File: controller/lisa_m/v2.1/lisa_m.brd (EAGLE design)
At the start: 50.7 x 33.6 mm, 119 parts, among them IC9 LP2992 5V, J1 CONN_3-1, J2 CONN_3-1, J3 CONN_3-1, J4 CONN_3-1, J5 CONN_3-1, J6 CONN_3-1, J7 CONN_3-1, J8 CONN_3-1, Q1 12Mhz, U1 MCP2551SN, U2 STM32-C-64, U3 BMP085

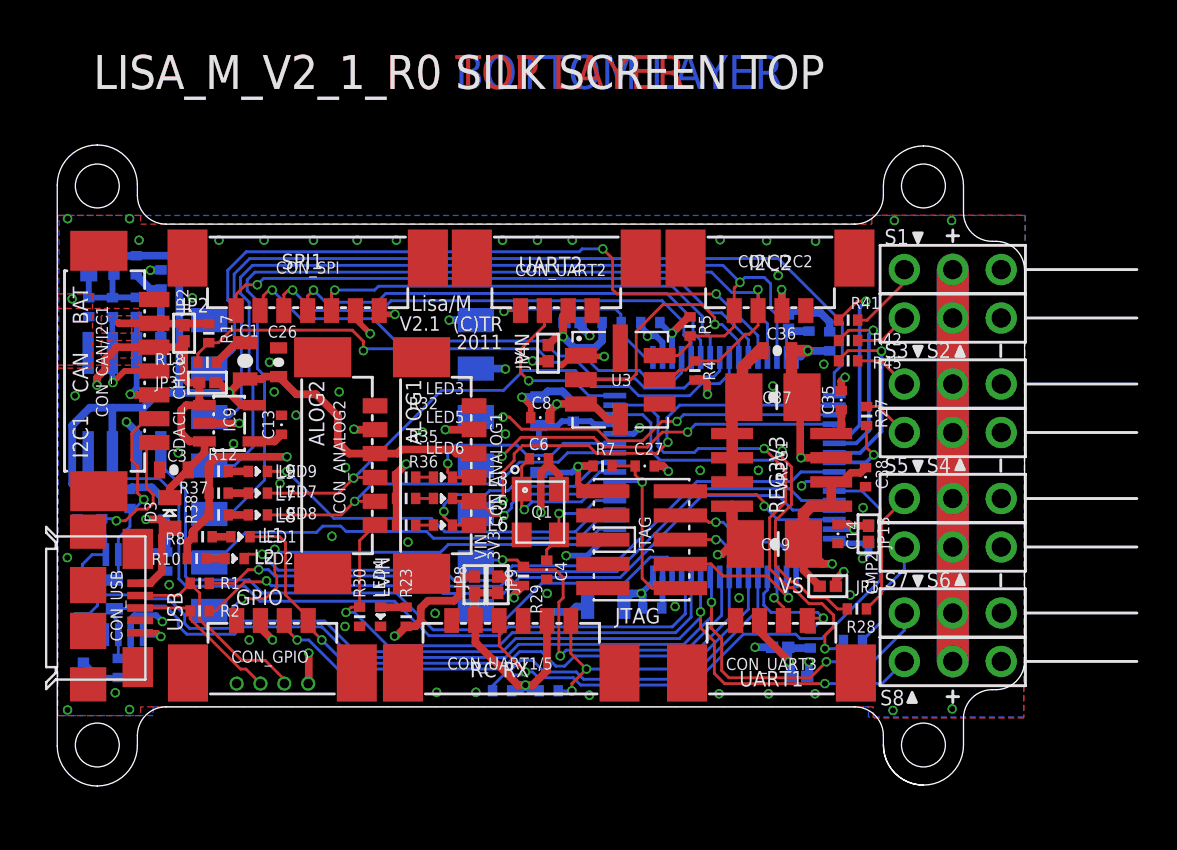
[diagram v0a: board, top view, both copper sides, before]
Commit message: Updated V2.1 Lisa/M(X) hardware to the final production version.
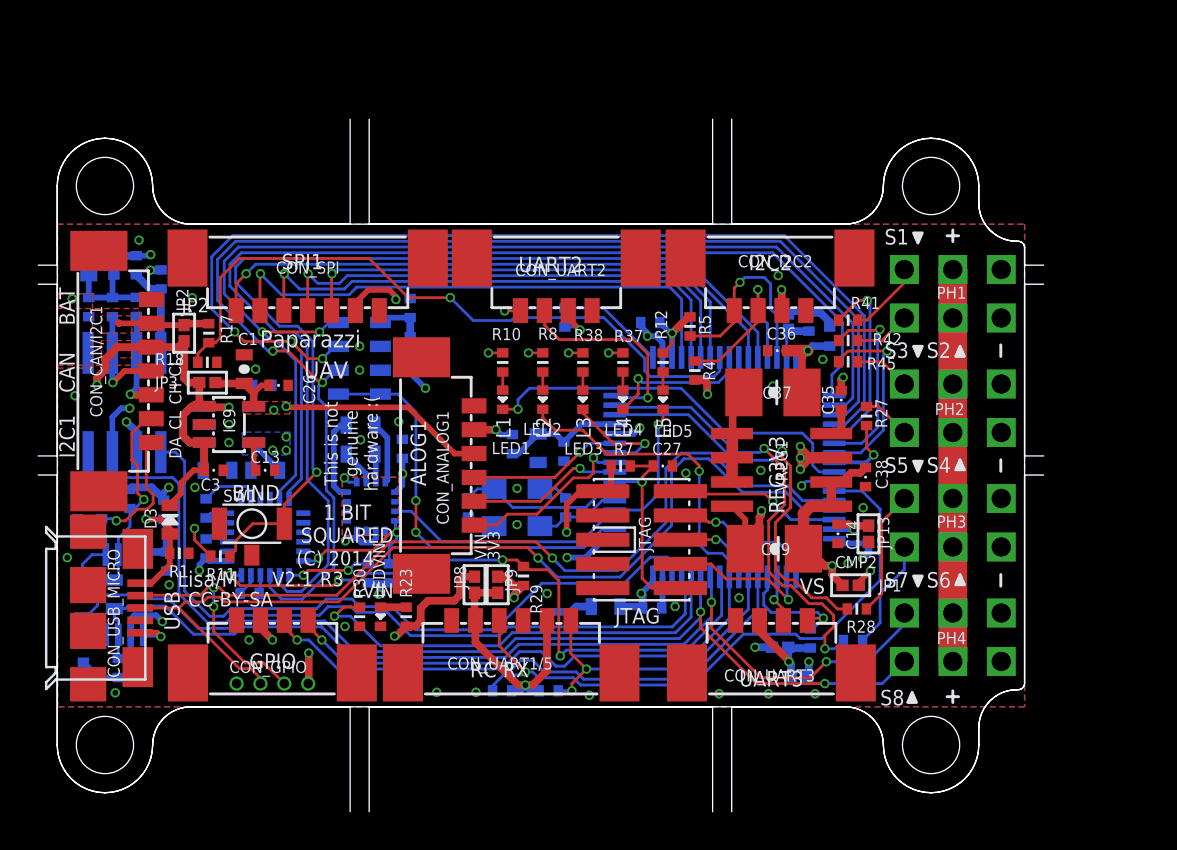
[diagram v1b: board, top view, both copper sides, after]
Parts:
- removed C8: 100n, pel_dipol_comp:0402-CAP
- removed CON_ANALOG2: (no value), pel_molex:PB-53398-06
- removed IMU: ASPIRIN, joby_robotics:ASPIRIN_1
- removed J1, J2, J3, J4, J5, J6, J7, J8: CONN_3-1, pel_misc:SIP1X3_100
- removed JP4, JP5: 0/DNP, pel_jumpers:0402-SQJMP
- removed LED6, LED7, LED8, LED9: BLU, pel_dipol_comp:0402-LED
- removed R32, R35, R36: 80R, pel_dipol_comp:0402-RES
- removed U$1: TR-LOGO, quadshot:TR-LOGO
- removed U3: BMP085, omc:LCC8
- added C101, C108, C110, C112: 100n, pel_dipol_comp:0402-CAP
- added C104: 2u2, pel_dipol_comp:0603-CAP
- added C105, C113: 4u7, pel_dipol_comp:0603-CAP
- added C106: 10n, pel_dipol_comp:0402-CAP
- added C109: 2n2, pel_dipol_comp:0402-CAP
- added C114: 220n, pel_dipol_comp:0603-CAP
- added IC101: LP2992, v-reg-micrel:SOT23-5
- added IC102: MS5611, aspirin:QFN-MS5611
- added L101: L, pel_dipol_comp:0402-IND
- added LEDVIN: GRN, pel_dipol_comp:0402-LED
- added PH1, PH2, PH3, PH4: PH2X3, pel_hdr:PH010-2-3
- added R11, R9: 2k2, pel_dipol_comp:0402-RES
- added SW1: MICROTACT_GND, paparazzi:MICROTACT_GND
- added U102: MPU-6000, aspirin:QFN24-NO-PAD
- added U103: HMC5883L, aspirin:LPCC16-HMC5883L
- C1, C9: device pel_dipol_comp:0805-CAP -> pel_dipol_comp:0603-CAP
- C26, C3, C36: device pel_dipol_comp:0603-CAP -> pel_dipol_comp:0402-CAP
- C28: device pel_dipol_comp:0603-POL-CAP -> pel_dipol_comp:0603-CAP
- C4, C6: value 30p -> 10p
- CON_CAN/I2C1: device pel_molex:PB-53261-07 -> pel_molex:PB-53398-07
- D3: device diode:MICROMELF-R -> pel_dipol_comp:0603-DIO
- L1: value (none) -> L; device res_cap:0603-IND -> pel_dipol_comp:0402-IND
- LED2: value BLU -> ORG
- LED3: value BLU -> GRN
- LED4: value ORG -> YEL
- LED5: value BLU -> RED
- R1: value 22R -> 10k
- R10, R12, R37, R38: value 80R -> 300
- R18, R23: value 2k -> 2k2
- R2: value 22R -> 2k2
- R24, R26, R29, R3, R30, R6: value 2k7 -> 10k
- R33, R34, R4, R5: value 2k7 -> 2k2
- R43, R44: value 1k5 -> 2k2
- R8: value 300R -> 300
- moved R12 24.0 mm to (31.8, 18.1), turned to 90 degrees
- moved R37 22.3 mm to (29.6, 18.1), turned to 90 degrees
- moved R38 20.7 mm to (27.6, 18.1), turned to 90 degrees
- moved R8 20.0 mm to (25.4, 18.1), turned to 90 degrees
- moved R10 19.0 mm to (23.4, 18.1), turned to 90 degrees
- moved LED2 18.2 mm to (25.4, 16.1), turned to 270 degrees
- moved LED4 17.1 mm to (29.6, 16.1)
- moved LED1 15.5 mm to (23.4, 16.1), turned to 270 degrees
- moved LED5 12.6 mm to (31.8, 16.1), turned to 270 degrees
- moved R2 10.1 mm to (17.4, 7.00), flipped to the bottom, turned to 270 degrees
- moved LED3 8.38 mm to (27.6, 16.1), turned to 270 degrees
- moved C6 4.49 mm to (21.6, 10.4), flipped to the bottom, turned to 270 degrees
- moved C4 3.41 mm to (26.6, 10.4), flipped to the bottom, turned to 270 degrees
- moved C13 2.53 mm to (10.9, 12.4), turned to 0 degrees
- moved R26 2.46 mm to (26.6, 20.4), turned to 90 degrees
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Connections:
- removed net ADC_4: CON_ANALOG2.4, LED7.C, U2.25
- removed net ADC_6: CON_ANALOG2.5, LED8.C, U2.10
- removed net FT_USB_DM: CON_USB.2, CON_USB_MICRO.PIN_2, R1.P$1
- removed net FT_USB_DP: CON_USB.3, CON_USB_MICRO.PIN_3, R2.P$1
- removed net IMU_ACC_CS: IMU.P$12, U2.33
- removed net IMU_ACC_DRDY: IMU.P$13, U2.28
- removed net IMU_GYRO_DRDY: IMU.P$9, U2.3
- removed net IMU_GYRO_SS: IMU.P$8, U2.2
- removed net IMU_MAG_DRDY: IMU.P$6, R29.P$2, U2.57
- removed net JTAG_TRST: CON_GPIO.4, LED1.C, U2.56
- removed net N$11: LED6.A, R36.P$1
- removed net N$9: LED5.A, R35.P$1
- removed net U2_POW: CON_UART2.2, JP4.P$2, JP5.P$2, R26.P$1
- new net BARO_+3V3: C101.P$1, IC102.1, L101.P$1
- new net BIND_BUT: R11.P$2, SW1.2, U2.28
- new net IMU+3V3: C105.P$1, C108.P$1, C112.P$1, IC101.5, L101.P$2, U102.13, U103.13, U103.2, U103.4
- new net IMU_BARO_CS: IC102.4, IC102.5, U2.2
- new net IMU_MAG_INT: U103.15, U2.3
- new net IMU_MPU_CS: U102.8, U2.33
- new net IMU_MPU_INT: R29.P$2, U102.12, U2.57
- new net LED3: LED3.C, U2.10
- new net LED4: LED4.C, U2.25
- new net LED5: LED5.C, U2.4
- new net N$19: C106.P$2, IC101.4
- new net N$2: C109.P$1, U102.20
- new net N$3: C110.P$1, U102.10
- new net N$34: C114.P$2, U103.8
- new net N$48: C114.P$1, U103.12
- new net SCL: R9.P$1, U102.7, U103.1
- new net SDA: R2.P$1, U102.6, U103.16
- net +3V3: now also CON_UART2.2, R11.P$1, R2.P$2, R26.P$1, R9.P$2; no longer C8.P$2, CON_ANALOG2.2, JP5.P$1, R32.P$2, R35.P$2, R36.P$2, U3.3, U3.4
- net +5V: no longer CON_ANALOG2.3
- net ADC_1: no longer LED3.C
- net ADC_2: no longer LED5.C
- net ADC_3: no longer LED6.C
- net BARO_DRDY: no longer U3.2
- net BOOT0: no longer CON_ANALOG2.6
- net GND: now also C101.P$2, C104.P$2, C105.P$2, C106.P$1, C108.P$2, C109.P$2, C110.P$2, C112.P$2, C113.P$2, C28.P$2, IC101.2, IC102.2, IC102.3, LEDVIN.C, PH1.3, PH1.6, PH2.3, PH2.6, PH3.3, PH3.6, PH4.3, PH4.6, R1.P$2, SW1.1, SW1.G, U102.1, U102.11, U102.18, U103.11, U103.9; no longer C28.-, C8.P$1, CON_ANALOG2.1, IMU.P$1, IMU.P$14, IMU.P$7, J1.1, J2.1, J3.1, J4.1, J5.1, J6.1, J7.1, J8.1, LED4.C, U3.1
- net I2C2_SCL: no longer IMU.P$10, U3.6
- net I2C2_SDA: no longer IMU.P$11, U3.7
- net IMU_SPI_MISO: now also IC102.6, U102.9; no longer IMU.P$3
- net IMU_SPI_MOSI: now also IC102.7, U102.24; no longer IMU.P$4
- net IMU_SPI_SCK: now also IC102.8, U102.23; no longer IMU.P$5
- net LED1: now also LED1.C; no longer LED2.C
- net LED2: now also CON_GPIO.4, LED2.C, U2.56; no longer LED9.C, U2.4
- net N$10: now also LED2.A; no longer LED1.A
- net N$12: now also LEDVIN.A; no longer LED4.A
- net N$13: now also LED5.A; no longer LED9.A
- net N$14: now also LED4.A; no longer LED7.A
- net N$15: now also LED3.A; no longer LED8.A
- net N$4: now also LED1.A; no longer LED2.A
- net N$5: now also C113.P$1, U103.10; no longer LED3.A, R32.P$1
- net S1: now also PH1.1; no longer J1.3
- net S2: now also PH1.4; no longer J2.3
- net S3: now also PH2.1; no longer J3.3
- net S4: now also PH2.4; no longer J4.3
- net S5: now also PH3.1; no longer J5.3
- net S6: now also PH3.4; no longer J6.3
- net S7: now also PH4.1; no longer J7.3
- net S8: now also PH4.4; no longer J8.3
- net SERVO_BUS: now also PH1.2, PH1.5, PH2.2, PH2.5, PH3.2, PH3.5, PH4.2, PH4.5; no longer J1.2, J2.2, J3.2, J4.2, J5.2, J6.2, J7.2, J8.2
- net USB_DM: now also CON_USB.2, CON_USB_MICRO.PIN_2; no longer R1.P$2
- net USB_DP: now also CON_USB.3, CON_USB_MICRO.PIN_3; no longer R2.P$2
- net USB_VBUS: now also R1.P$1
- net VDDA: now also C28.P$1; no longer C28.+
- net V_IN: now also C104.P$1, IC101.1, IC101.3; no longer IMU.P$2, JP4.P$1
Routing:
- net IMU_MPU_CS: track 0.00 -> 60.2 mm
- net BIND_BUT: track 0.00 -> 50.8 mm, vias 0 -> 1
- net IMU_SPI_MISO: track 19.9 -> 67.1 mm
- net IMU_ACC_CS: track 46.6 -> 0.00 mm
- net I2C2_SCL: track 53.9 -> 9.61 mm
- net IMU_SPI_MOSI: track 20.1 -> 62.6 mm, vias 2 -> 3
- net I2C2_SDA: track 51.7 -> 10.7 mm
- net IMU_ACC_DRDY: track 38.3 -> 0.00 mm, vias 2 -> 0
- net IMU_SPI_SCK: track 23.4 -> 58.6 mm
- net IMU_MPU_INT: track 0.00 -> 34.4 mm, vias 0 -> 4
- net JTAG_TRST: track 33.5 -> 0.00 mm, vias 1 -> 0
- net ADC_4: track 29.9 -> 0.00 mm, vias 1 -> 0
- net IMU_GYRO_SS: track 24.5 -> 0.00 mm, vias 2 -> 0
- net +5V: track 49.1 -> 25.5 mm, vias 1 -> 5
- net LED2: track 20.0 -> 43.6 mm, vias 1 -> 2
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- added copper zone on layer 1, net +5V
- added copper zone on layer 15, net +5V
- added copper zone on layer 15, net IMU+3V3
- added copper zone on layer 16, net IMU+3V3
- added copper zone on layer 1, net N$11
- added copper zone on layer 15, net N$11
- added copper zone on layer 16, net N$11
- added copper zone on layer 2, net N$11
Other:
- board size 50.7 x 33.6 mm -> 52.7 x 36.3 mm
- board text added: "(C) 2010-2015 Piotr Esden-Tempski <piotr@esden.net>"
- board text added: "(C) 2014"
- board text added: "(C)1B2"
- board text added: "1 BIT SQUARED"
- board text added: "2014"
- board text added: "BIND"
- board text added: "CC-BY-SA"
- board text added: "CON_USB_MICRO"
- board text added: "D3 SHOT"
- board text added: "L4"
- board text added: "R3"
- board text added: "RX1"
- board text added: "SO8 3V3"
- board text added: "SOT23-5 3V3"
- board text added: "SOT23-5 5V"
- board text added: "This is not genuine hardware :("
- board text added: "UART3"
- board text removed: "(C) 2010-2011 Antoine Drouin <poinix@gmail.com>"
- board text removed: "(C) 2010-2011 Piotr Esden-Tempski <piotr@esden.net>"
- board text removed: "(C) 2011 Joby Robotics <info@jobyrobotics.com>"
- board text removed: "(C) 2011 Richard Hatano <rhatano@jobyenergy.com>"
- board text removed: "(C) 2011 Transition Robotics <info@transition-robotics.com>"
- board text removed: "(C)TR"
- board text removed: "2011"
- board text removed: "25.3mm"
- board text removed: "47mm"
- board text removed: "ACC_CS"
- board text removed: "ACC_DRDY"
- board text removed: "ALOG2"
- board text removed: "ASPIRIN_IMU"
- board text removed: "CON_USB"
- board text removed: "GYRO_DRDY"
- board text removed: "GYRO_SS"
- board text removed: "L6"
- board text removed: "L7"
- board text removed: "L8"
- board text removed: "L9"
- board text removed: "LISA_M_V1_1_R0 SOLDER MASK BOTTOM"
- board text removed: "LISA_M_V1_1_R0 SOLDER MASK TOP"
- board text removed: "LISA_M_V1_1_R0 SOLDER PASTE BOTTOM"
- board text removed: "LISA_M_V1_1_R0 SOLDER PASTE TOP"
- board text removed: "LISA_M_V1_R0 DRILL LEGEND"
- board text removed: "LISA_M_V2_1_R0 BOTTOM LAYER"
- board text removed: "LISA_M_V2_1_R0 LAYER 2"
- board text removed: "LISA_M_V2_1_R0 LAYER 3"
- board text removed: "LISA_M_V2_1_R0 SILK SCREEN BOTTOM"
- board text removed: "LISA_M_V2_1_R0 SILK SCREEN TOP"
- board text removed: "LISA_M_V2_1_R0 TOP LAYER"
- board text removed: "MAG_DRDY"
- board text removed: "RX3"
- board text removed: "Robotics"
- board text removed: "Transition"
- board text removed: "UART1"
